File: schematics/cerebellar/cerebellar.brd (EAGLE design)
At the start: 108.6 x 91.1 mm, 69 parts, among them CON2 ODrive1, CON4 Odrive3, CON5 ODrive4, CON6 Odrive2, CON7 ODrive5, CON8 ODrive6, IC2 SN75C3232, IC3 LTC7001, P1 Foot1, P10 SPI2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

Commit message: no message
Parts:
- removed C18, C2, C3, C4: 100nF, rcl:C025-025X050
- removed C7: 1nF, rcl:C025-025X050
- removed IC2: SN75C3232, MAX3232:SOIC16
- removed R11: 100k, rcl:0204/7
- added P14: IMU, jst-ph:JST-PH5
- added R8: 1K, rcl:0204/7
- P15: value Switch -> ON
- P4: value IMU -> LED; device jst-ph:JST-PH6 -> jst-ph:JST-PH2
- R1: value 10K -> 6.8k
- U$4: value MCP1725-ADJE/SN -> MAX769L; device MCP1725-ADJE_SN:SOIC127P599X175-8N -> MAX869:TSSOP-16
- moved U2 67.5 mm to (29.2, 59.7)
- moved R5 56.6 mm to (33.7, 59.7)
- moved R2 56.6 mm to (36.2, 59.7), turned to 270 degrees
- moved R1 54.7 mm to (74.3, 75.6)
- moved P4 48.9 mm to (85.1, 76.2)
- moved U$4 46.4 mm to (67.9, 75.6)
- moved IC3 37.6 mm to (43.8, 59.7)
- moved R10 36.5 mm to (50.8, 59.7)
- moved R4 36.5 mm to (53.3, 59.7)
- moved C19 32.0 mm to (39.4, 59.7), turned to 90 degrees
- moved R7 26.9 mm to (48.3, 59.7)
- moved R9 23.6 mm to (58.4, 59.7)
- moved R15 23.6 mm to (55.9, 59.7)
- moved R20 21.5 mm to (41.9, 36.2)
- moved C26 20.3 mm to (38.7, 36.2)
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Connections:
- removed net IMU-D+: P4.3
- removed net IMU_D-: P4.4
- removed net IMU_RX: IC2.P$14, P4.1
- removed net IMU_TX: IC2.P$13, P4.2
- removed net N$11: C2.1, IC2.P$4
- removed net N$12: C2.2, IC2.P$5
- removed net N$13: C4.1, IC2.P$2
- removed net N$14: C3.1, IC2.P$6
- removed net N$25: R1.1, R11.2, U$4.7
- removed net N$7: U$1.9-OUT1C, U$4.3
- removed net N$8: C18.2, IC2.P$3
- removed net VOUT_IMU: IC2.P$16, P4.5, R11.1, U$4.8
- new net N$2: R1.1, U$4.9
- net +5V: now also P14.4, U$4.12, U$4.13, U$4.16, U$4.4, U$4.5; no longer U$4.2
- net GND: now also P14.5, P4.2, U$4.8; no longer C3.2, C4.2, C7.2, IC2.P$15, P4.6, U$4.4
- net IMU_VDD: now also P14.1; no longer U$4.5
- net LED_PWM: now also U$4.7
- net N$3: now also P4.1, R8.2; no longer C7.1, U$4.6
- net N$6: now also R8.1, U$4.11, U$4.14, U$4.15, U$4.2, U$4.3, U$4.6; no longer C18.1, IC2.P$1
- net T_RX: now also P14.3; no longer IC2.P$12
- net T_TX: now also P14.2; no longer IC2.P$11
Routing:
- net VOUT_IMU: track 119.9 -> 0.00 mm
- net GND: track 510.7 -> 414.1 mm, vias 3 -> 1
- net N$5: track 114.9 -> 40.2 mm
- net N$18: track 89.2 -> 17.7 mm, vias 0 -> 2
- net LED_PWM: track 0.00 -> 69.6 mm, vias 0 -> 1
- net V+: track 85.5 -> 26.9 mm, vias 2 -> 0
- net IMU_VDD: track 27.3 -> 83.2 mm
- net N$10: track 106.4 -> 55.9 mm, vias 3 -> 0
- net T_TX: track 33.6 -> 75.4 mm, vias 1 -> 0
- net SENS3: track 114.0 -> 72.5 mm, vias 0 -> 1
- net IMU_TX: track 37.5 -> 0.00 mm
- net SENS4: track 113.9 -> 78.7 mm, vias 2 -> 1
- net IMU_RX: track 35.2 -> 0.00 mm, vias 2 -> 0
- net +5V: track 212.3 -> 244.5 mm, vias 5 -> 4
- net N$23: track 98.7 -> 128.9 mm
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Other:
- board size 108.6 x 91.1 mm -> 98.4 x 91.1 mm

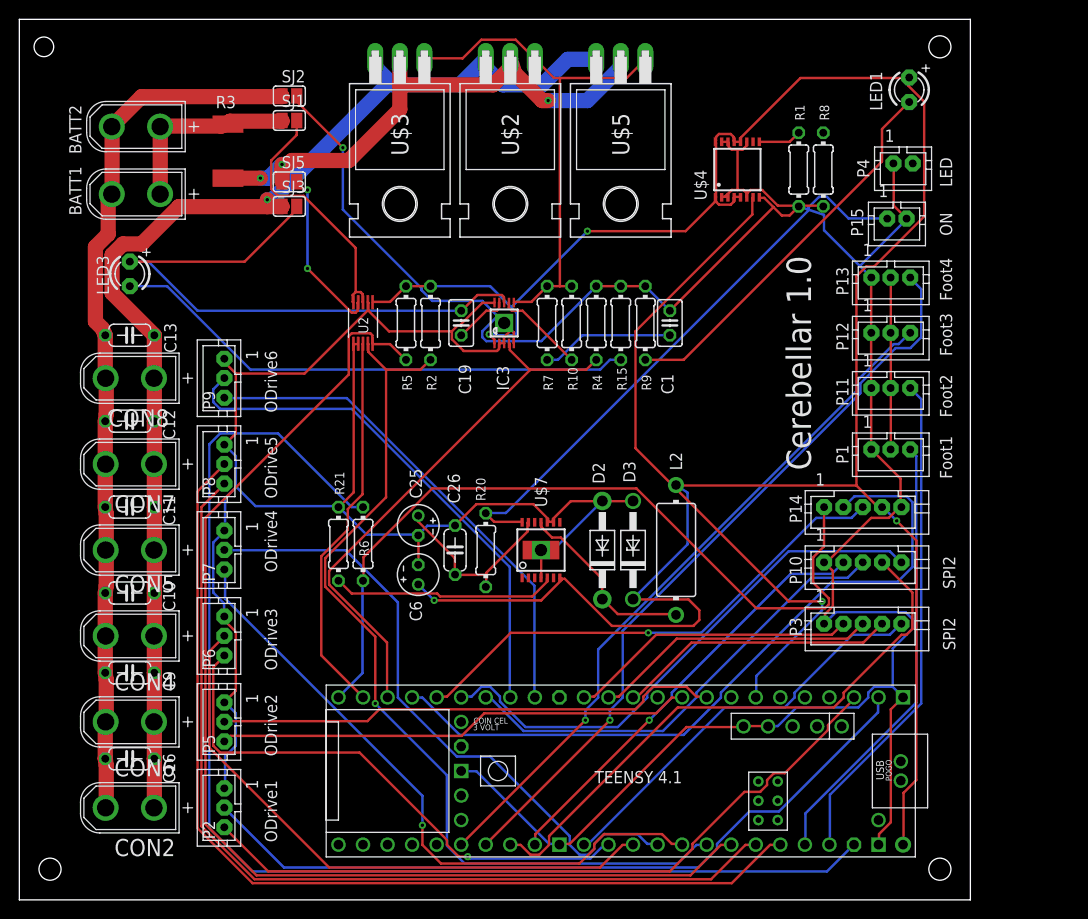
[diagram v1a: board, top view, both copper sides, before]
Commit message: added magnetssensor
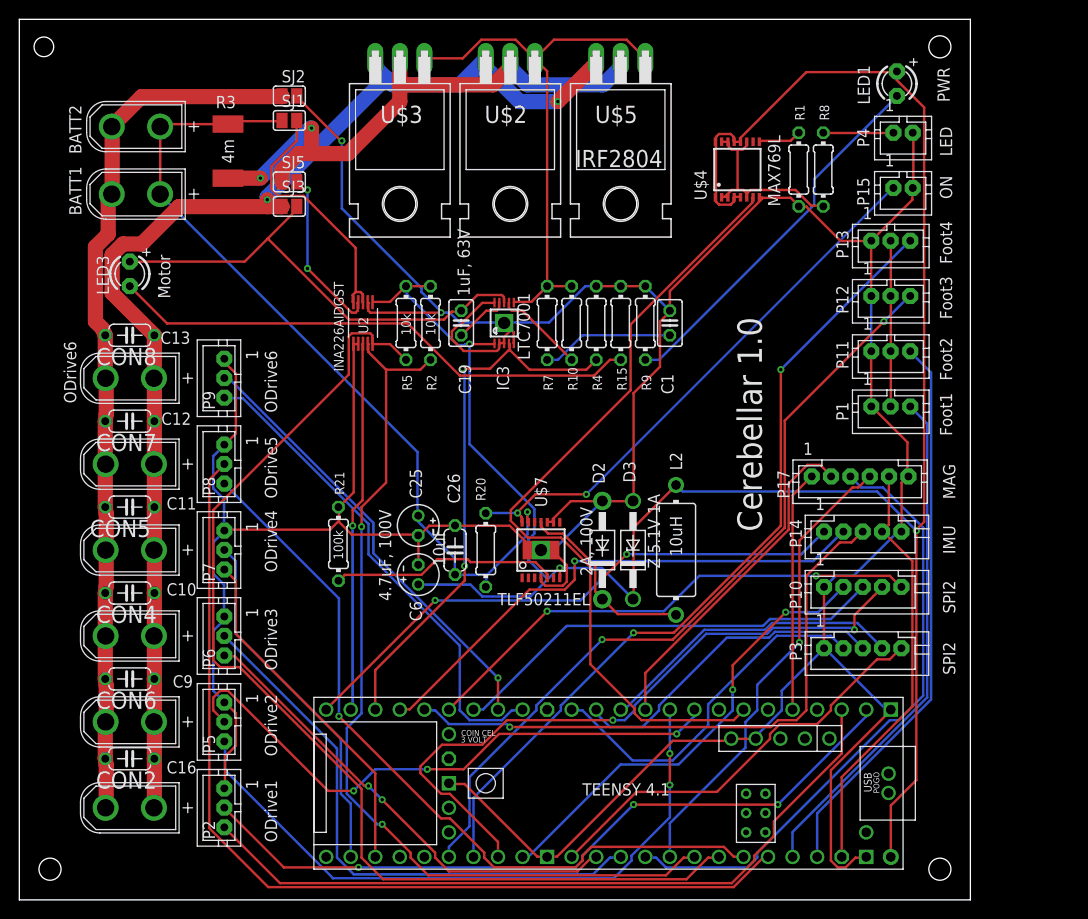
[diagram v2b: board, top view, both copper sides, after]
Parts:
- removed R6: 100k, rcl:0204/7
- added P17: MAG, jst-ph:JST-PH6
- LED1: value ON -> PWR
- LED3: value Mot ON -> Motor
- moved P1 4.45 mm to (83.8, 49.5)
- moved P12 3.81 mm to (83.8, 61.0)
- moved P11 3.81 mm to (83.8, 55.2)
- moved P13 3.81 mm to (83.8, 66.7)
- moved P15 3.24 mm to (85.1, 73.7)
- moved P4 3.17 mm to (85.1, 79.4)
- moved P10 2.54 mm to (81.9, 32.4)
- moved P14 2.54 mm to (81.9, 38.1)
- moved P3 2.54 mm to (81.9, 26.0)
- moved U$1 1.80 mm to (53.3, 12.1)
- moved LED1 1.42 mm to (84.5, 84.5)
- moved C9 0.64 mm to (5.08, 22.9)
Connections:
- net PWR_BATT- renamed BATT-
- removed net IMU_VDD: P14.1, R6.1, U$1.32-OUT1B
- removed net N$23: R6.2, U$1.3V3-3
- removed net PWR_BATT+: BATT1.+, BATT2.+, R3.1, SJ1.1
- new net IMU_ENABLE: P14.1, U$1.32-OUT1B
- new net MAG_EN: P17.2, U$1.9-OUT1C
- new net MAG_INT: P17.1, U$1.3-LRCLK2
- new net MAG_SCL: P17.3, U$1.16-A2/RX4/SCL1
- new net MAG_SDA: P17.4, U$1.17-A3/TX4/SDA1
- new net UC3.3V: P14.4, P17.5, U$1.3V3-3
- net +5V: no longer P14.4
- net BATT+: now also BATT1.+, BATT2.+, R3.1, SJ1.1
- net GND: now also P17.6
- net O4_RX: now also U$1.34-RX8; no longer U$1.16-A2/RX4/SCL1
- net O4_TX: now also U$1.35-TX8; no longer U$1.17-A3/TX4/SDA1
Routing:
- net N$23: track 128.9 -> 0.00 mm
- net IMU_VDD: track 83.2 -> 0.00 mm
- net BATT+: track 19.4 -> 86.0 mm, vias 0 -> 1
- net MAG_SCL: track 0.00 -> 64.0 mm
- net IMU_ENABLE: track 0.00 -> 59.2 mm, vias 0 -> 3
- net MAG_SDA: track 0.00 -> 48.3 mm, vias 0 -> 1
- net UC3.3V: track 0.00 -> 44.1 mm
- net MAG_EN: track 0.00 -> 35.2 mm
- net O4_TX: track 66.7 -> 36.2 mm, vias 1 -> 0
- net O4_RX: track 65.8 -> 37.2 mm
- net MAG_INT: track 0.00 -> 25.0 mm
- net T_TX: track 75.4 -> 54.7 mm, vias 0 -> 1
- net PWR_BATT+: track 19.9 -> 0.00 mm
- net O2_TX: track 49.2 -> 67.7 mm, vias 0 -> 2
- net O5_TX: track 97.5 -> 79.2 mm, vias 0 -> 1
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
